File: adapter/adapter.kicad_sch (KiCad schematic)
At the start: 14 parts, among them J10 Ribbon, J11 Ribbon, J12 Ribbon, J2 DF3A-2P-2DSA, J9 Ribbon, SW1 SW_Push, SW2 CAS-120TA, U1 nice_nano, U2 nice_nano

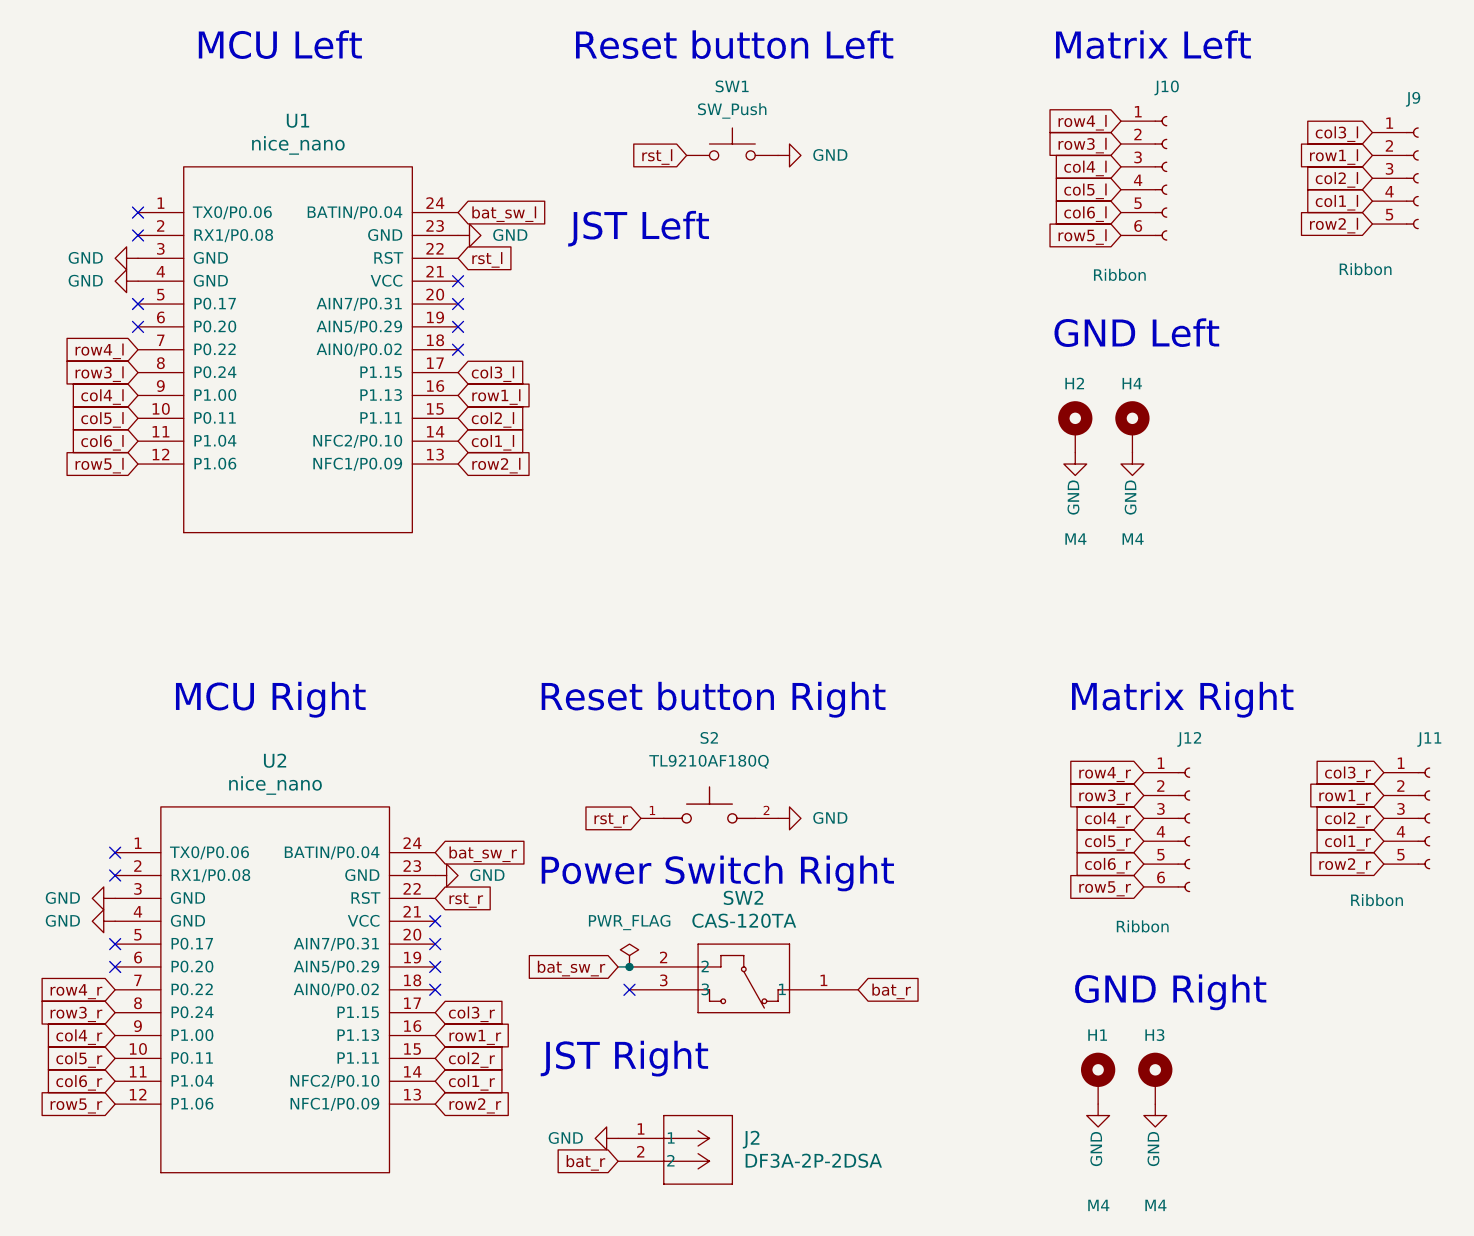
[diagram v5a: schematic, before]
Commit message: Add JST connectors and cleaned up the PCB
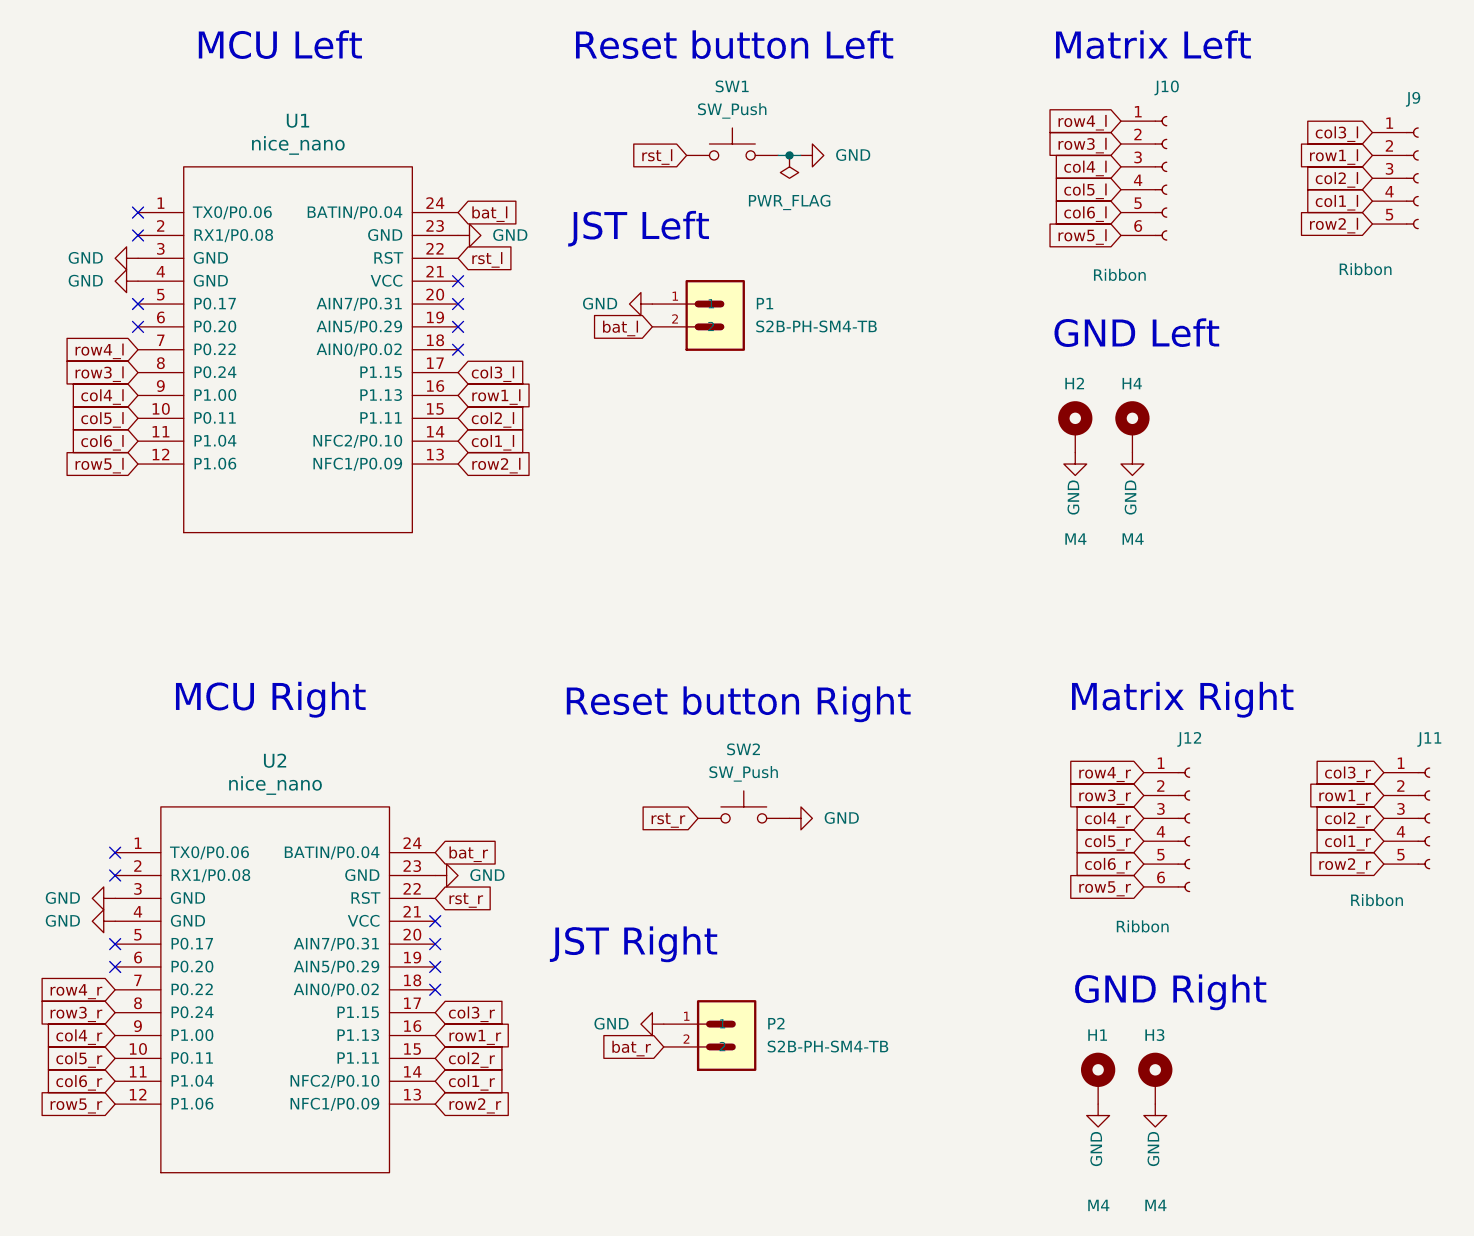
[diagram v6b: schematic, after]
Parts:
- removed J2: DF3A-2P-2DSA, Library:DF3A_2P_2DSA, symbol DF3A_2P_2DSA:DF3A-2P-2DSA
- removed S2: TL9210AF180Q, Library:SW_TL9210AF180Q, symbol TL9210AF180Q:TL9210AF180Q
- removed SW2: CAS-120TA, Library:CAS-120A_NDC, symbol CAS-120TA:CAS-120TA
- added P1, P2: S2B-PH-SM4-TB, Library:JST_S2B-PH-SM4-TB, symbol S2B-PH-SM4-TB:S2B-PH-SM4-TB
- added SW2: SW_Push, Library:SW_Tactile_3x3_SMD_H1p5, symbol Switch:SW_Push
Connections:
- net bat_sw_r is gone; now on net bat_r: U2.24 (BATIN/P0.04)
- net GND: now also P1.1, P2.1, SW2.2
- net bat_r: now also P2.2
- net rst_r: now also SW2.1
- net bat_sw_l renamed bat_l
- net bat_l: now also P1.2
- no-connect marks 17 -> 16
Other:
- note removed: "Power Switch Right"
